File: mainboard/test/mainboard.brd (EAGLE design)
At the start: 66 x 38.1 mm, 110 parts, among them Q1 MOSFET-NCHANNEL2N7002PW, Q2 MOSFET-NCHANNEL2N7002PW, Q3 MOSFET-NCHANNEL2N7002PW, Q4 BSS84, Q5 BSS84, Q7 MOSFET-NCHANNEL2N7002PW

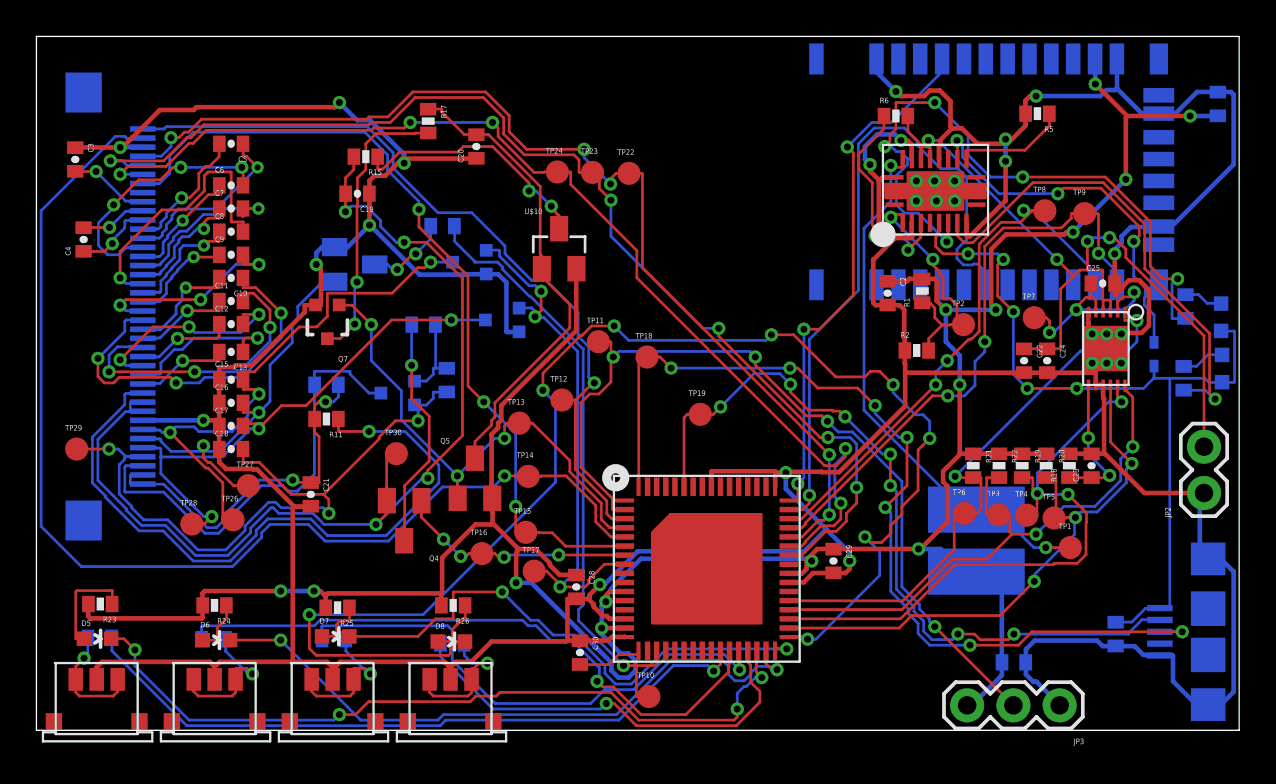
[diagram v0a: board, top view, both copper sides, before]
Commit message: created a back up board
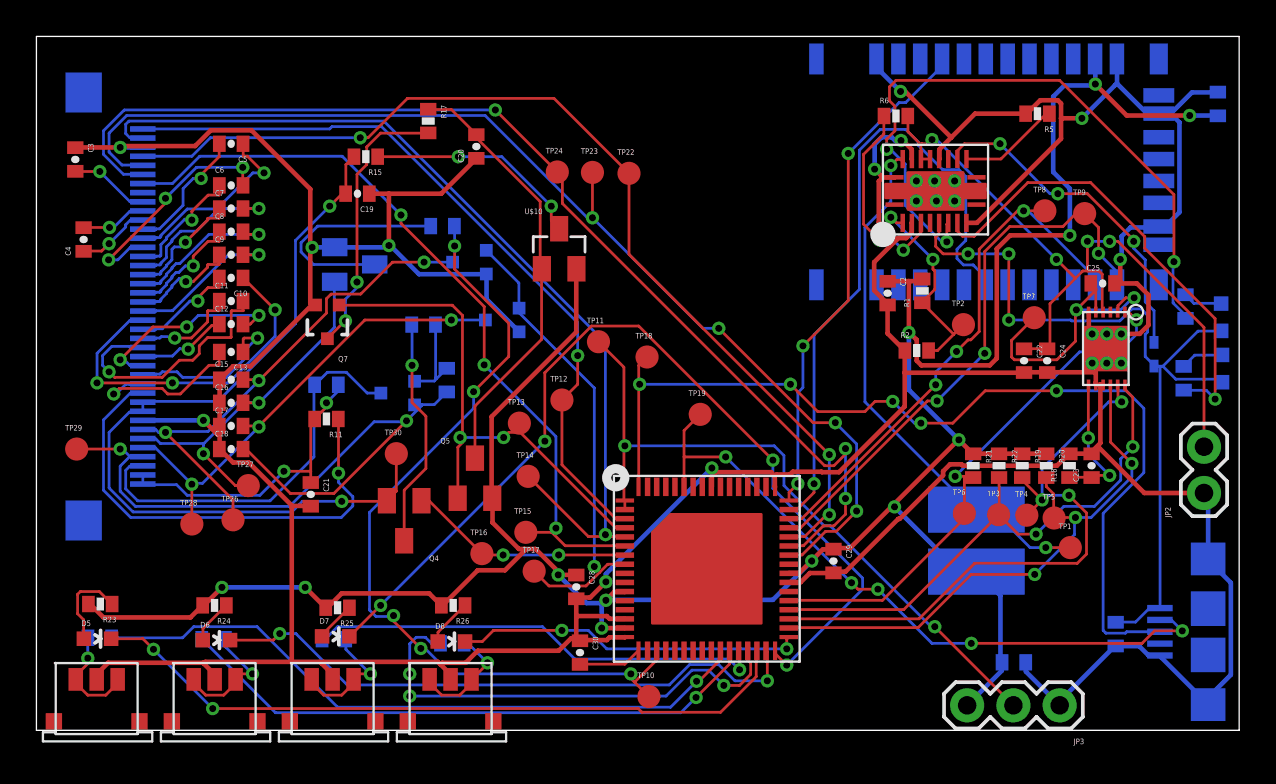
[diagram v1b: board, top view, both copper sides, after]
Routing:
- net LED_3: track 76.8 -> 19.0 mm, vias 8 -> 2
- net LED_2: track 29.7 -> 51.6 mm, vias 2 -> 4
- net EPD_BUSY: track 62.5 -> 50.4 mm
- net VCOM_DRIVER: track 38.1 -> 26.3 mm
- net EPD_PWM: track 33.9 -> 45.4 mm, vias 1 -> 5
- net VCC_T: track 57.1 -> 45.7 mm, vias 4 -> 2
- net GND: track 304.6 -> 295.3 mm, vias 16 -> 11
- net SENSOR_DATA: track 47.1 -> 38.1 mm, vias 4 -> 2
- net N$9: track 4.60 -> 12.3 mm, vias 2 -> 0
- net N$34: track 15.2 -> 8.66 mm
- net VCC: track 154.4 -> 149.1 mm, vias 14 -> 12
- net VCC_R: track 12.0 -> 16.9 mm, vias 3 -> 2
- net SPYBY_TEST: track 42.6 -> 37.7 mm, vias 7 -> 5
- net N$45: track 5.21 -> 9.49 mm
- net VCOM: track 20.3 -> 16.5 mm
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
